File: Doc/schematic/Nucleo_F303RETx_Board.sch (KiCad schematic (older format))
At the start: 35 parts, among them CN1 CONN_01X10, CN2 CONN_01X08, CN3 CONN_02X19, CN4 CONN_02X19, CN5 CONN_01X08, CN6 CONN_01X06, P10 Serial, P11 Rotary Encoder Board, P12 Power Board, P13 Basis, P8 KTY81-110, P9 LCD Board, Q8 BD135, Q9 BD135, U3 93CxxA, U4 CA3140

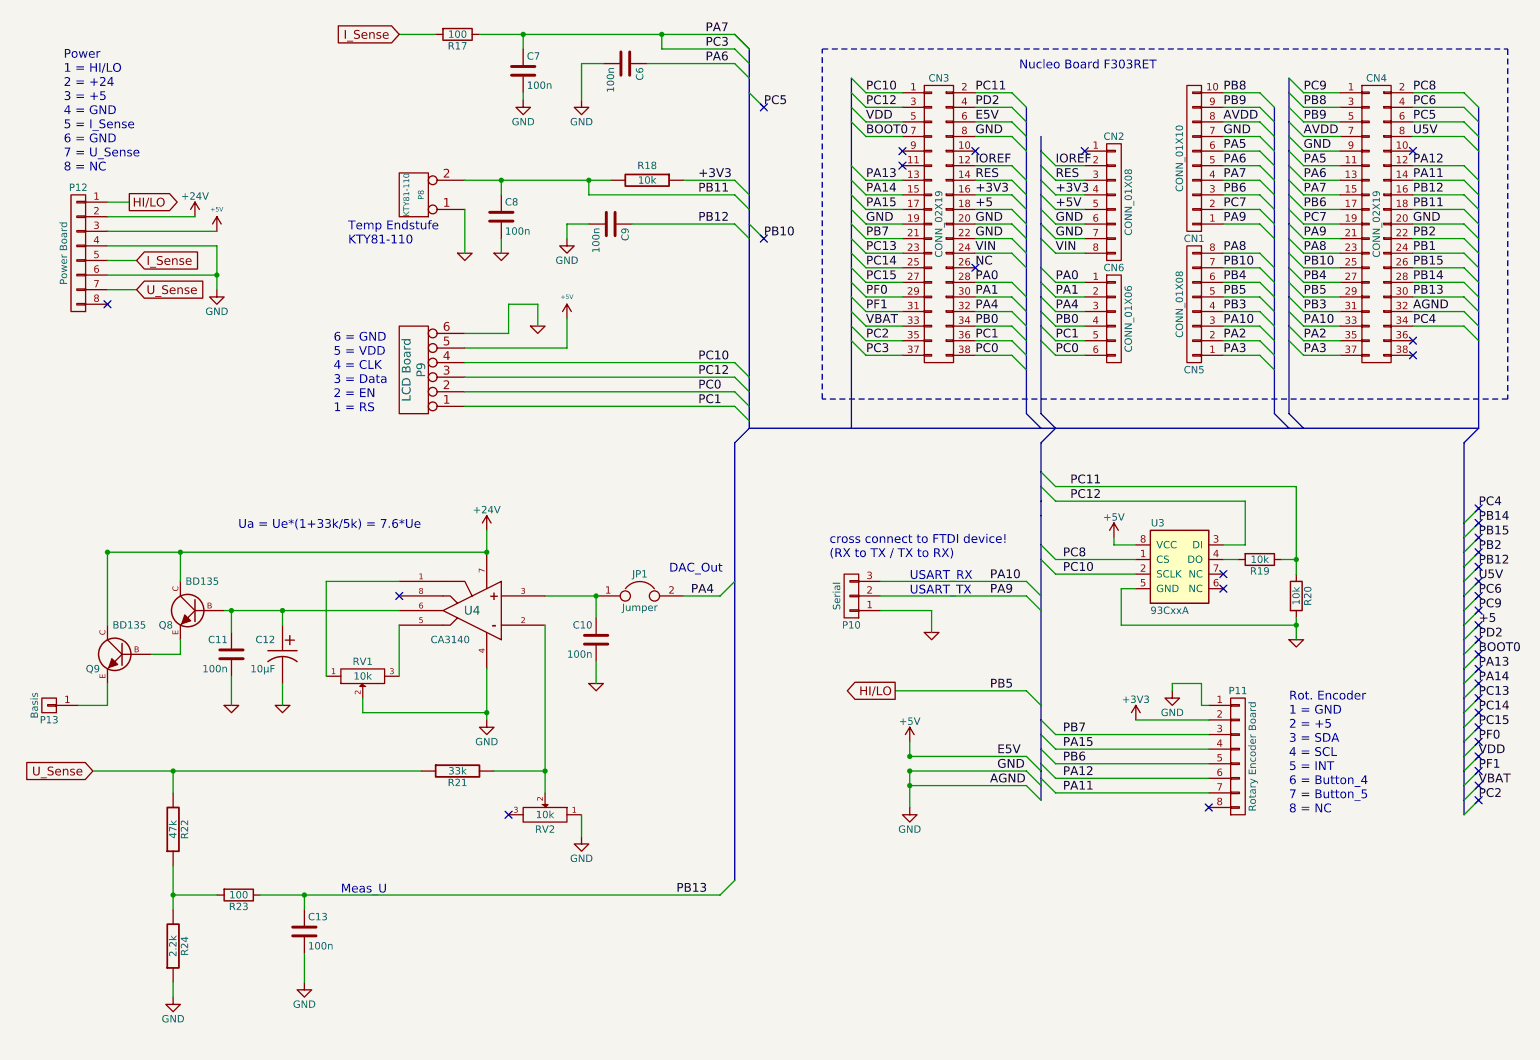
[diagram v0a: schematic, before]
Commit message: Measurements and measurement-display first version finished.
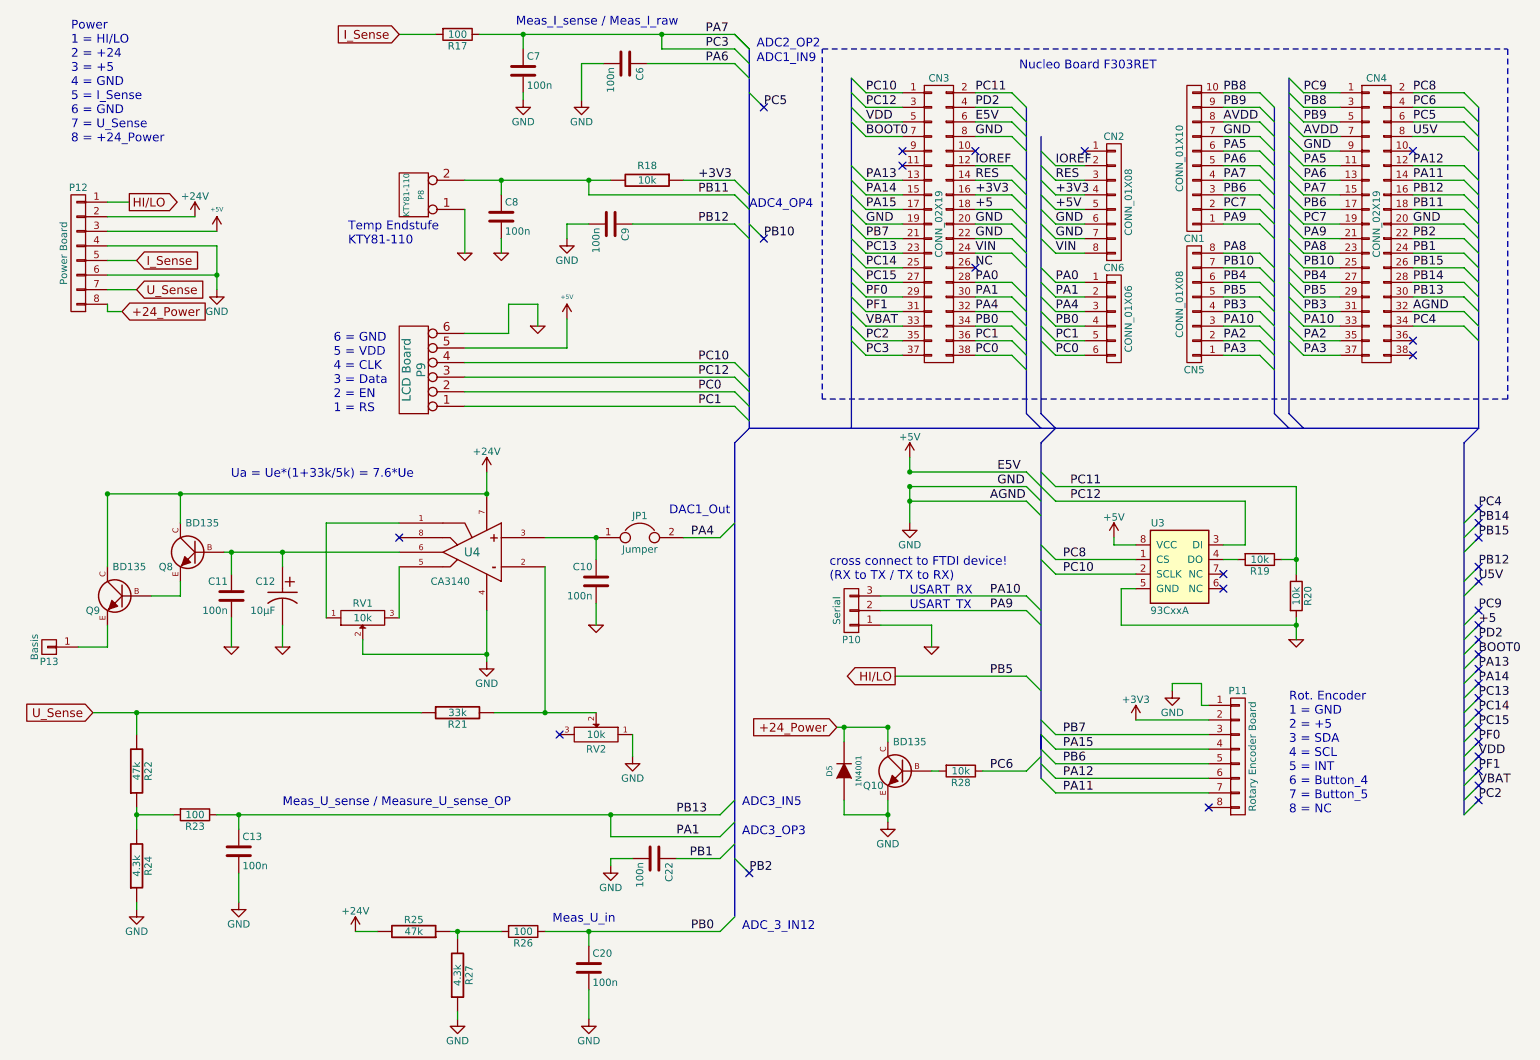
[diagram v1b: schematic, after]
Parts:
- added C20, C22: 100n, symbol C
- added D5: 1N4001, symbol DIODE
- added Q10: BD135, symbol BC237-RESCUE-Netzteil_Progammable
- added R25: 47k, symbol R-RESCUE-Netzteil_Progammable
- added R26: 100, symbol R
- added R27: 4.3k, symbol R-RESCUE-Netzteil_Progammable
- added R28: 10k, symbol R
- R24: value 2.2k -> 4.3k
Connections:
- net PB13 is gone; now on net PA1: C13.1, CN4.30 (P30), R23.1
- net +24V: now also R25.2
- net GND: now also C20.2, C22.2, D5.1 (A), Q10.E, R27.1
- net PB0: now also C20.1, R26.1
- net PB1: now also C22.1
- net PC6: now also R28.1
- net +24_Power: now reaches P12.8 (P8)
- net +24_Power: now also D5.2 (K), Q10.C
- new net: R25.1, R26.2, R27.2
- new net: Q10.B, R28.2
- no-connect marks 37 -> 35
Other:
- note added: "ADC1_IN9"
- note added: "ADC2_OP2"
- note added: "ADC3_IN5"
- note added: "ADC3_OP3"
- note added: "ADC4_OP4"
- note added: "ADC_3_IN12"
- note added: "DAC1_Out"
- note added: "Meas_I_sense / Meas_I_raw"
- note added: "Meas_U_in"
- note added: "Meas_U_sense / Measure_U_sense_OP"
- note added: "Power\n1 = HI/LO\n2 = +24\n3 = +5\n4 = GND\n5 = I_Sense\n6 = GND\n7 = U_Sense\n8 = +24_Power"
- note removed: "DAC_Out"
- note removed: "Meas_U"
- note removed: "Power\n1 = HI/LO\n2 = +24\n3 = +5\n4 = GND\n5 = I_Sense\n6 = GND\n7 = U_Sense\n8 = NC"
- moved on the sheet: C10, C11, C12, C13, JP1, P10, P13, Q8, Q9, R21, R22, R23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

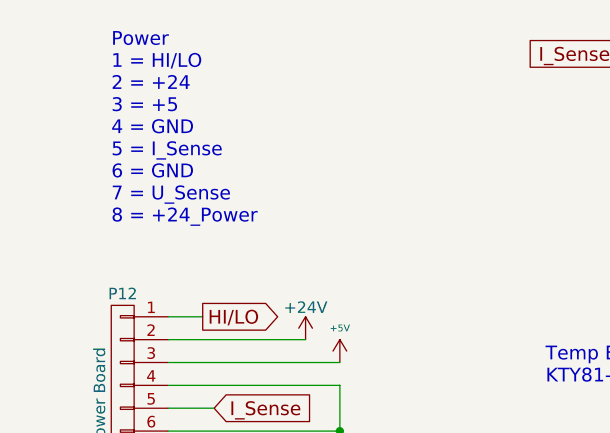
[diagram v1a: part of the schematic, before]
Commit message: Outputting voltage works. Measurement voltage works, not yet calibrated.
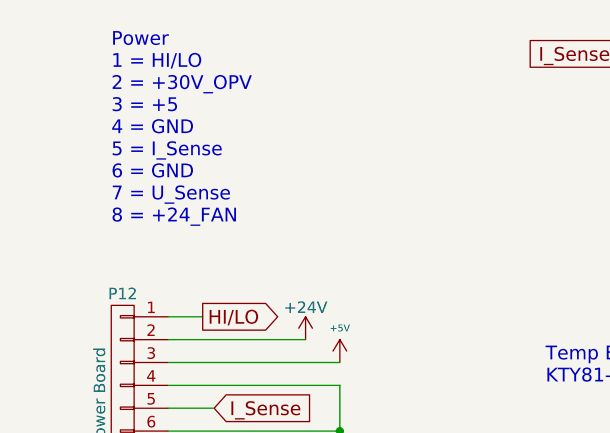
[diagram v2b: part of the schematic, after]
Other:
- note added: "Power\n1 = HI/LO\n2 = +30V_OPV\n3 = +5\n4 = GND\n5 = I_Sense\n6 = GND\n7 = U_Sense\n8 = +24_FAN"
- note removed: "Power\n1 = HI/LO\n2 = +24\n3 = +5\n4 = GND\n5 = I_Sense\n6 = GND\n7 = U_Sense\n8 = +24_Power"
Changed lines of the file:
@@
 	6550 4750 7550 4750
 $Comp
-L GND-RESCUE-Netzteil_Progammable #PWR40
+L GND-RESCUE-Netzteil_Progammable #PWR45
 U 1 1 5897DA08
 P 6900 5000
-F 0 "#PWR40" H 6900 5000 30  0001 C CNN
+F 0 "#PWR45" H 6900 5000 30  0001 C CNN
 F 1 "GND" H 6900 4930 30  0001 C CNN
 F 2 "" H 6900 5000 60  0001 C CNN
@@
 $EndComp
 $Comp
-L GND-RESCUE-Netzteil_Progammable #PWR43
+L GND-RESCUE-Netzteil_Progammable #PWR44
 U 1 1 58992617
 P 2450 5000
-F 0 "#PWR43" H 2450 5000 30  0001 C CNN
+F 0 "#PWR44" H 2450 5000 30  0001 C CNN
 F 1 "GND" H 2450 4930 30  0001 C CNN
 F 2 "" H 2450 5000 60  0001 C CNN
@@
 	9400 3900 9400 4500
 $Comp
-L GND-RESCUE-Netzteil_Progammable #PWR41
+L GND-RESCUE-Netzteil_Progammable #PWR42
 U 1 1 589B7E9E
 P 9400 4950
-F 0 "#PWR41" H 9400 4950 30  0001 C CNN
+F 0 "#PWR42" H 9400 4950 30  0001 C CNN
 F 1 "GND" H 9400 4880 30  0001 C CNN
 F 2 "" H 9400 4950 60  0001 C CNN
@@
 PC11
 $Comp
-L +5V #PWR38
+L +5V #PWR40
 U 1 1 589BC9EE
 P 8150 4250
-F 0 "#PWR38" H 8150 4100 50  0001 C CNN
+F 0 "#PWR40" H 8150 4100 50  0001 C CNN
 F 1 "+5V" H 8150 4390 50  0000 C CNN
 F 2 "" H 8150 4250 50  0000 C CNN
@@
 $EndComp
 $Comp
-L GND-RESCUE-Netzteil_Progammable #PWR39
+L GND-RESCUE-Netzteil_Progammable #PWR41
 U 1 1 589BF775
 P 4600 4850
-F 0 "#PWR39" H 4600 4850 30  0001 C CNN
+F 0 "#PWR41" H 4600 4850 30  0001 C CNN
 F 1 "GND" H 4600 4780 30  0001 C CNN
 F 2 "" H 4600 4850 60  0001 C CNN
@@
 $EndComp
 $Comp
-L GND-RESCUE-Netzteil_Progammable #PWR42
+L GND-RESCUE-Netzteil_Progammable #PWR43
 U 1 1 589C0F0C
 P 2100 5000
-F 0 "#PWR42" H 2100 5000 30  0001 C CNN
+F 0 "#PWR43" H 2100 5000 30  0001 C CNN
 F 1 "GND" H 2100 4930 30  0001 C CNN
 F 2 "" H 2100 5000 60  0001 C CNN
@@
 NoConn ~ 4350 5600
 $Comp
-L GND #PWR48
+L GND #PWR49
 U 1 1 589D160B
 P 4850 5750
-F 0 "#PWR48" H 4850 5500 50  0001 C CNN
+F 0 "#PWR49" H 4850 5500 50  0001 C CNN
 F 1 "GND" H 4850 5600 50  0000 C CNN
 F 2 "" H 4850 5750 50  0000 C CNN
@@
 $EndComp
 $Comp
-L +24V #PWR37
+L +24V #PWR38
 U 1 1 589D1CF3
 P 3850 3800
-F 0 "#PWR37" H 3850 3650 50  0001 C CNN
+F 0 "#PWR38" H 3850 3650 50  0001 C CNN
 F 1 "+24V" H 3850 3940 50  0000 C CNN
 F 2 "" H 3850 3800 50  0000 C CNN
@@
 $EndComp
 $Comp
-L GND #PWR44
+L GND #PWR46
 U 1 1 589D21CF
 P 3850 5100
-F 0 "#PWR44" H 3850 4850 50  0001 C CNN
+F 0 "#PWR46" H 3850 4850 50  0001 C CNN
 F 1 "GND" H 3850 4950 50  0000 C CNN
 F 2 "" H 3850 5100 50  0000 C CNN
@@
 NoConn ~ 3250 4250
 $Comp
-L +5V #PWR46
+L +5V #PWR37
 U 1 1 589D3582
 P 6750 3700
-F 0 "#PWR46" H 6750 3550 50  0001 C CNN
+F 0 "#PWR37" H 6750 3550 50  0001 C CNN
 F 1 "+5V" H 6750 3840 50  0000 C CNN
 F 2 "" H 6750 3700 50  0000 C CNN
@@
 Connection ~ 6750 3800
 $Comp
-L GND #PWR50
+L GND #PWR39
 U 1 1 589D373E
 P 6750 4150
-F 0 "#PWR50" H 6750 3900 50  0001 C CNN
+F 0 "#PWR39" H 6750 3900 50  0001 C CNN
 F 1 "GND" H 6750 4000 50  0000 C CNN
 F 2 "" H 6750 4150 50  0000 C CNN
@@
 $EndComp
 $Comp
-L +3V3 #PWR47
+L +3V3 #PWR48
 U 1 1 589EAFA5
 P 8300 5500
-F 0 "#PWR47" H 8300 5350 50  0001 C CNN
+F 0 "#PWR48" H 8300 5350 50  0001 C CNN
 F 1 "+3V3" H 8300 5640 50  0000 C CNN
 F 2 "" H 8300 5500 50  0000 C CNN
@@
 $EndComp
 $Comp
-L GND #PWR45
+L GND #PWR47
 U 1 1 589EAFAB
 P 8550 5300
-F 0 "#PWR45" H 8550 5050 50  0001 C CNN
+F 0 "#PWR47" H 8550 5050 50  0001 C CNN
 F 1 "GND" H 8550 5150 50  0000 C CNN
 F 2 "" H 8550 5300 50  0000 C CNN
@@
 $EndComp
 Text Notes 1000 1550 0    60   ~ 0
-Power\n1 = HI/LO\n2 = +24\n3 = +5\n4 = GND\n5 = I_Sense\n6 = GND\n7 = U_Sense\n8 = +24_Power
+Power\n1 = HI/LO\n2 = +30V_OPV\n3 = +5\n4 = GND\n5 = I_Sense\n6 = GND\n7 = U_Sense\n8 = +24_FAN
 Text GLabel 1450 2350 2    60   Input ~ 0
 I_Sense
@@
 $EndComp
 $Comp
-L GND #PWR54
+L GND #PWR56
 U 1 1 58FE65EF
 P 4550 7550
-F 0 "#PWR54" H 4550 7300 50  0001 C CNN
+F 0 "#PWR56" H 4550 7300 50  0001 C CNN
 F 1 "GND" H 4550 7400 50  0000 C CNN
 F 2 "" H 4550 7550 50  0000 C CNN
@@
 $EndComp
 $Comp
-L +24V #PWR51
+L +24V #PWR54
 U 1 1 58FE6EEA
 P 2950 6950
-F 0 "#PWR51" H 2950 6800 50  0001 C CNN
+F 0 "#PWR54" H 2950 6800 50  0001 C CNN
 F 1 "+24V" H 2950 7090 50  0000 C CNN
 F 2 "" H 2950 6950 50  0000 C CNN
@@
 $EndComp
 $Comp
-L GND #PWR56
+L GND #PWR50
 U 1 1 58FEC241
 P 6600 6200
-F 0 "#PWR56" H 6600 5950 50  0001 C CNN
+F 0 "#PWR50" H 6600 5950 50  0001 C CNN
 F 1 "GND" H 6600 6050 50  0000 C CNN
 F 2 "" H 6600 6200 50  0000 C CNN
@@
 $EndComp
 $Comp
-L GND #PWR49
+L GND #PWR51
 U 1 1 5A3D4FBC
 P 4700 6500
-F 0 "#PWR49" H 4700 6250 50  0001 C CNN
+F 0 "#PWR51" H 4700 6250 50  0001 C CNN
 F 1 "GND" H 4700 6350 50  0000 C CNN
 F 2 "" H 4700 6500 50  0000 C CNN
